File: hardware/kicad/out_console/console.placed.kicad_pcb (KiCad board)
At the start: 2 copper layers, 99.5 x 99.5 mm, 62 parts, among them J1 RaspberryPi_Pico_SMD_HandSold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, J10 JST_XH_B2B-XH-A_1x02_P2.50mm_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, J11 JST_XH_B2B-XH-A_1x02_P2.50mm_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, J12 JST_XH_B2B-XH-A_1x02_P2.50mm_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, J13 JST_XH_B2B-XH-A_1x02_P2.50mm_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, J14 JST_XH_B2B-XH-A_1x02_P2.50mm_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, J15 JST_XH_B2B-XH-A_1x02_P2.50mm_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, J16 JST_XH_B2B-XH-A_1x02_P2.50mm_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, J17 JST_XH_B2B-XH-A_1x02_P2.50mm_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, J18 JST_XH_B2B-XH-A_1x02_P2.50mm_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, J19 JST_XH_B2B-XH-A_1x02_P2.50mm_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, J2 IDC-Header_2x20_P2.54mm_Verti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, J20 JST_XH_B3B-XH-A_1x03_P2.50mm_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, J21 JST_XH_B3B-XH-A_1x03_P2.50mm_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, J22 PinHeader_2x04_P2.54mm_Vertic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, J3 JST_XH_B4B-XH-A_1x04_P2.50mm_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, J4 JST_XH_B3B-XH-A_1x03_P2.50mm_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, J5 JST_XH_B2B-XH-A_1x02_P2.50mm_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, J6 JST_XH_B4B-XH-A_1x04_P2.50mm_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, J7 JST_XH_B3B-XH-A_1x03_P2.50mm_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, J8 JST_XH_B2B-XH-A_1x02_P2.50mm_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, J9 JST_XH_B2B-XH-A_1x02_P2.50mm_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, U1 DIP-14_W7.62mm, U2 DIP-6_W7.62mm

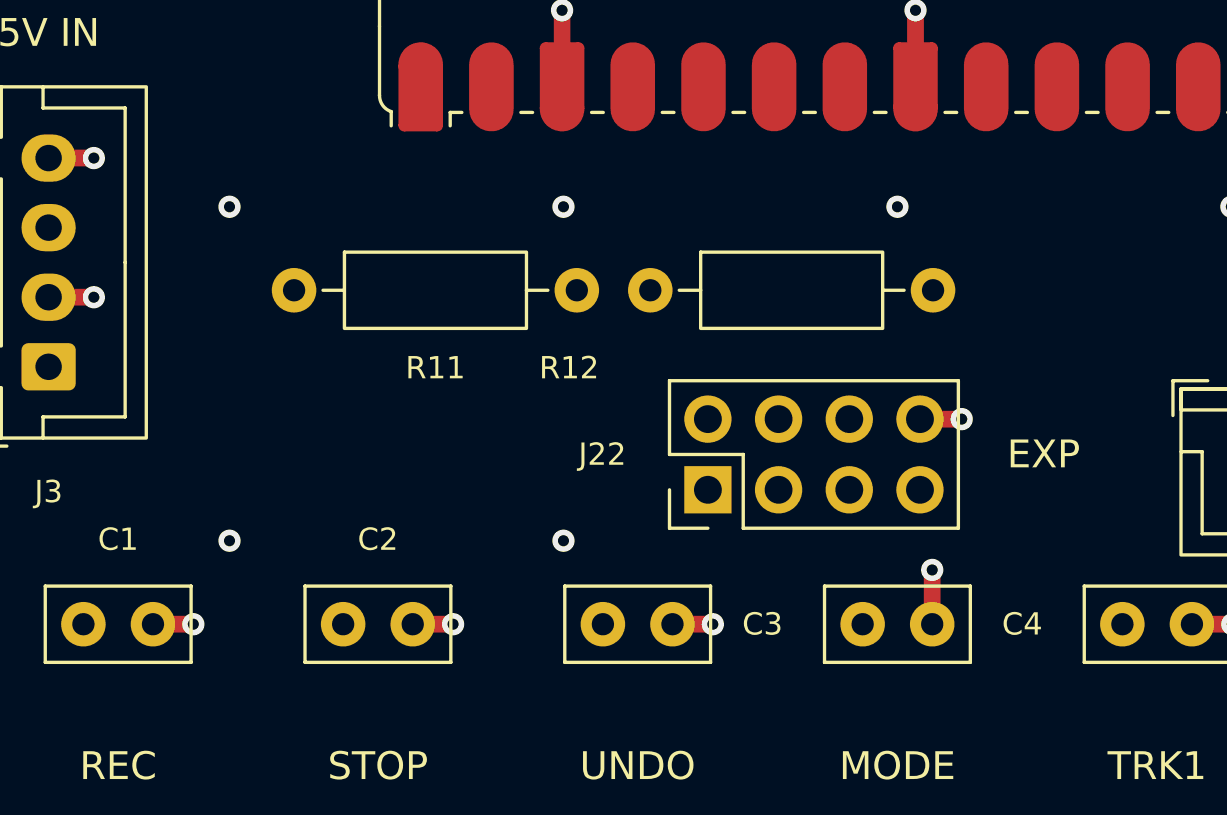
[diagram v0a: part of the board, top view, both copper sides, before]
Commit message: feat(hardware): console board v3 — read the PD trigger's contract over I2C
The console cannot tell whether the STUSB4500 negotiated 20 V / 5 A or a
65 W brick's 20 V / 3.25 A: both boot, and the second browns out only when
the LEDs go white under two lit screens. The chip is I2C-readable (RDO at
0x91-0x94 with capaMismatch, voltage at 0x21), so v3 gives it a header.

J23 PD: JST-XH 3-way — GND, SDA, SCL on GP0/GP1 (I2C0, the pins v2 left
spare), under the module's left end beside 5V IN; R11/R12 rise 3 mm to make
the row. Three wires on purpose: the breakout's VDD and pull-ups come off
VBUS on its own board, and this board's 3V3 is downstream of the contract
being measured. A gate now asserts the pair is one I2C instance's SDA/SCL,
and no GPIO on the module is spare any more (the UART self-test that leaned
on GP1 being free swaps pins instead).

Routed clean: 0 DRC violations, 0 unconnected, ratsnest 1725 mm of 1770.
Silk keep-outs and back art regenerated for the new pad set.

Firmware for the read and its pedal-link report is not written yet; the
wiring doc, the soldering guide's v3 table and the firmware README say so.
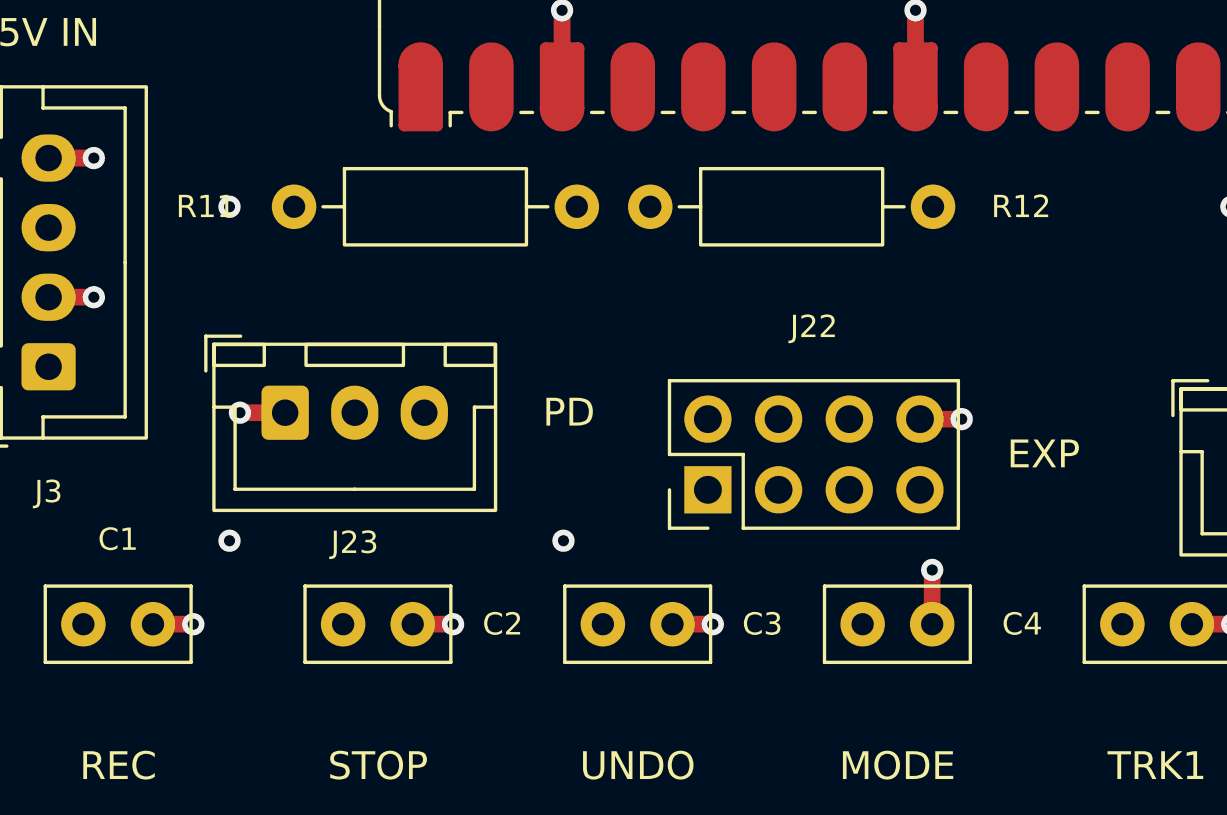
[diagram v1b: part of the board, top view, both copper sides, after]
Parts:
- added J23: JST_XH_B3B-XH-A_1x03_P2.50mm_Vertical, JST_XH_B3B-XH-A_1x03_P2.50mm_Vertical, F.Cu at (114.0, 127.4)
- moved R11 3.00 mm to (114.3, 120.0)
- moved R12 3.00 mm to (127.1, 120.0)
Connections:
- J1 pad 1: (no net) -> PD_SDA
- J1 pad 2: (no net) -> PD_SCL
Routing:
- net GND: track 117.8 -> 119.4 mm, vias 75 -> 74
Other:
- board text added: "PD"

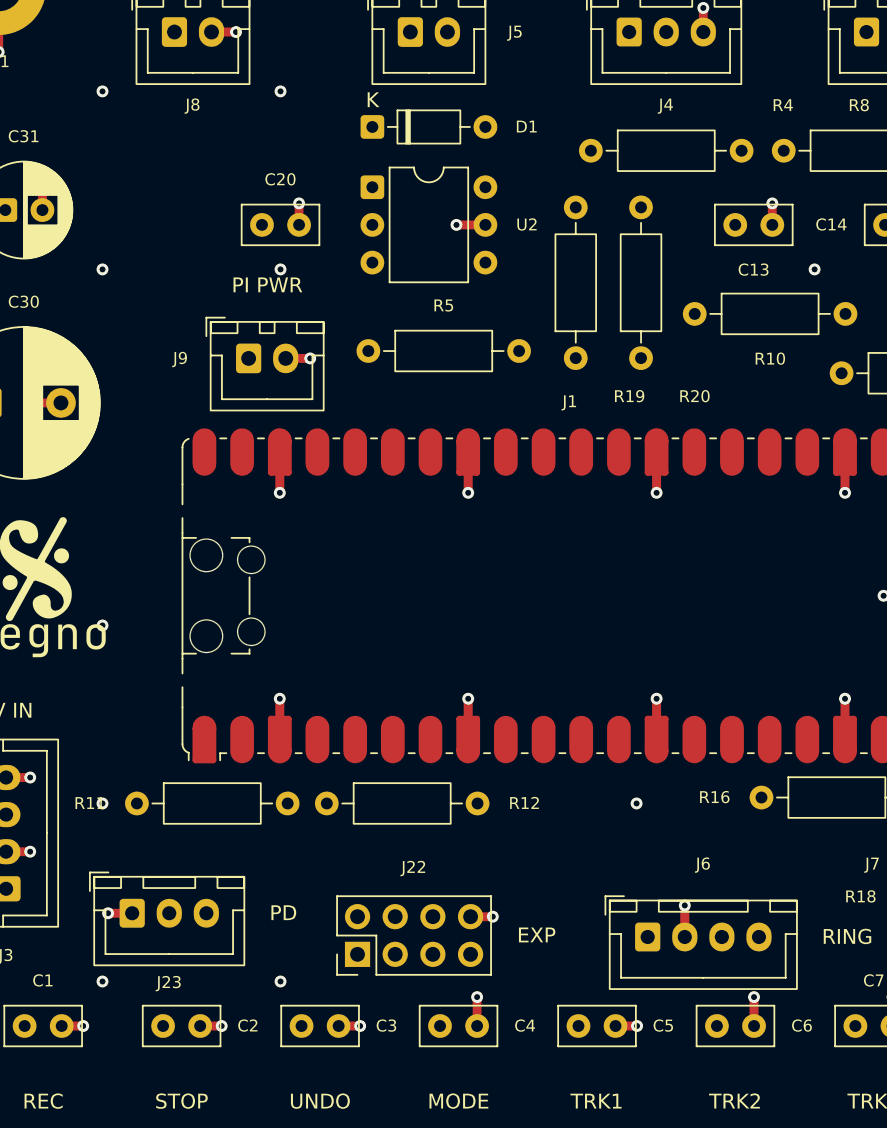
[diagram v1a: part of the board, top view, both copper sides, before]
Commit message: fix(hardware): v3 — EXP back where v2 had it, PD in the RING row
Bench feedback on the v3 layout: the expansion header was liked where v2 put
it, and the PD header sat 1.6 mm above the row it belongs to.

J22 returns to the column beside U2. R19/R20, which had taken that column
to stay under the jacks, move to the row R13 and R15 left empty under the
module; their nets are DC sense lines through 4.7 k, so the 50-60 mm run
does not matter, and the hop gate exempts them by name with that reason
(SLOW_SENSE_NETS). J23 drops onto the RING/LEDS row.

The silk keep-out list now covers every pad that opens the back mask, not
only plated ones: the Pico's three NPTH anchors were missed and the big
segno landed on them (silk_over_copper). Routed clean: 0 violations,
0 unconnected, ratsnest 1707 mm of 1770. Gerbers regenerated.
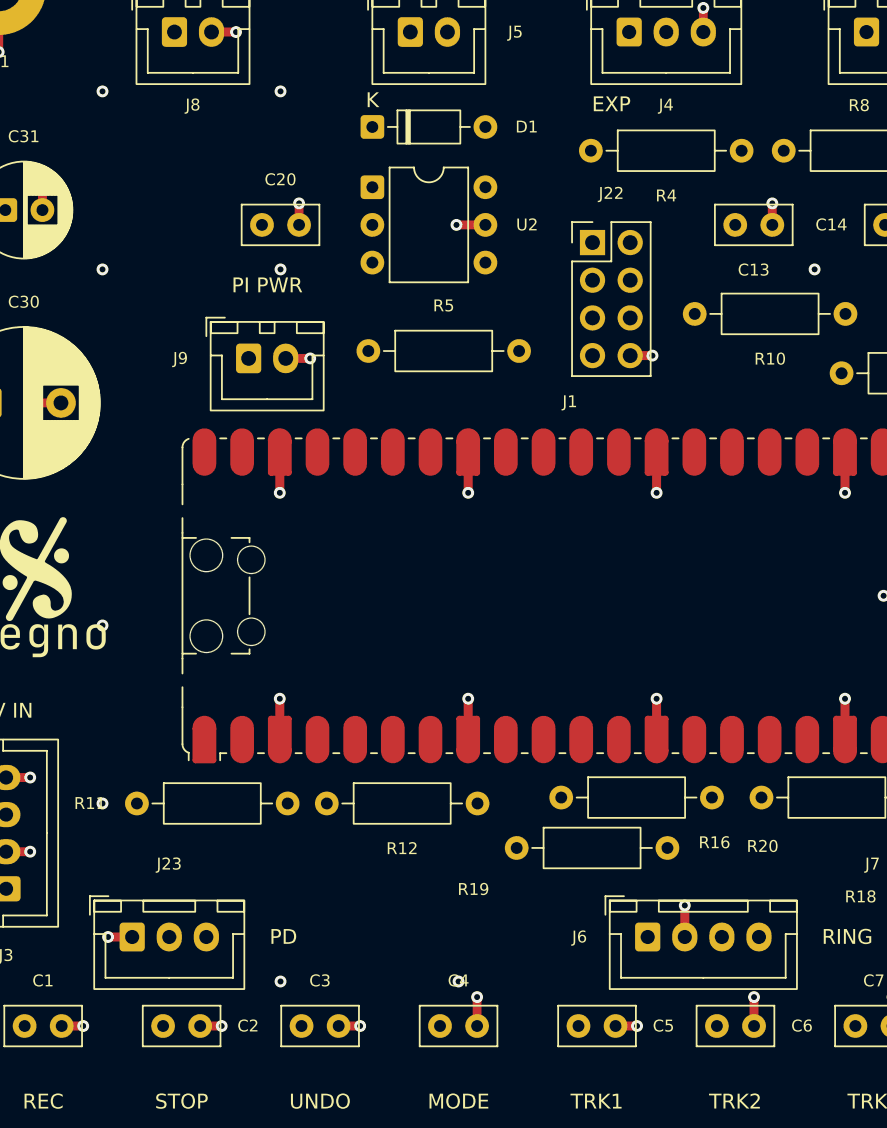
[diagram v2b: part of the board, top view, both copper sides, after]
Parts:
- moved J22 50.5 mm to (145.0, 82.2), turned to 0 degrees
- moved R19 33.3 mm to (139.9, 123.0), turned to 0 degrees
- moved R20 30.1 mm to (142.9, 119.6), turned to 0 degrees
- moved J23 1.60 mm to (114.0, 129.0)
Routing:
- net GND: vias 74 -> 73

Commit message: feat(hardware): console board v3 — switched CTRL jacks report presence
The CTRL jacks become Neutrik NJ6FD-V: D-series like the jack they
replace, same Ø24 punch and M3 pair, with switching contacts. Each jack's
tip-normal contact goes to the board as a fourth lead (J20/J21 are 4-way
now) and through 4.7 k (R21/R22) to GP19/GP22. The contact ties to the
tip — 3V3 through 10 k — while the jack is empty and opens once a plug is
in, so with the RP2350's pull-down the pin is high only for an empty jack.
Presence becomes a wire: an empty jack no longer reads as a pedal at full
toe, and a plug on its way in is ignored until it is seated. Firmware 1.2
reads it; on a v2 board the same pins float on J22's pads and read
"plugged", so one firmware serves both.

GP19/GP22 leave J22, which is 2x3 (GP12, GP15, GP28). The CTRL headers
slide 2.6 mm left to keep their clearances at 4-way width; R11/R12 join
R16/R20 on the band under the module so the row below is R21/R22's.

Ratsnest 1915 mm: the four sense nets run 50-60 mm to parts under the
module by decision (DC through 4.7 k, exempt from the hop gate), so the
budget follows the measurement to 2050 with that reason next to it. Routed
clean: 0 violations, 0 unconnected. Gerbers, BOM and art regenerated.

Docs: shopping list (NJ6FD-V x2, four leads), soldering guide's v3 table,
wiring, firmware README pin table.
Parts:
- added R21: R_Axial_DIN0207_L6.3mm_D2.5mm_P10.16mm_Horizontal, R_Axial_DIN0207_L6.3mm_D2.5mm_P10.16mm_Horizontal, F.Cu at (111.9, 123.0)
- added R22: R_Axial_DIN0207_L6.3mm_D2.5mm_P10.16mm_Horizontal, R_Axial_DIN0207_L6.3mm_D2.5mm_P10.16mm_Horizontal, F.Cu at (124.9, 123.0)
- J20, J21: value JST_XH_B3B-XH-A_1x03_P2.50mm_Vertical -> JST_XH_B4B-XH-A_1x04_P2.50mm_Vertical; footprint JST_XH_B3B-XH-A_1x03_P2.50mm_Vertical -> JST_XH_B4B-XH-A_1x04_P2.50mm_Vertical
- J22: value PinHeader_2x04_P2.54mm_Vertical -> PinHeader_2x03_P2.54mm_Vertical; footprint PinHeader_2x04_P2.54mm_Vertical -> PinHeader_2x03_P2.54mm_Vertical
- moved J20 3.85 mm to (159.7, 68.0)
- moved J21 1.55 mm to (173.9, 68.0)
- moved J22 1.27 mm to (145.0, 83.5)
- moved R11 0.40 mm to (114.3, 119.6)
- moved R12 0.40 mm to (127.1, 119.6)
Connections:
- J1 pad 25: EXP_GP19 -> CTRL1_PRESENT
- J1 pad 29: EXP_GP22 -> CTRL2_PRESENT
- J22 pad 5: EXP_GP19 -> EXP_GP28
- J22 pad 6: EXP_GP22 -> GND

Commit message: refactor(hardware): the issue numbers come off the console silkscreen
The bottom strip printed "SEGNO CONSOLE v3  #747 #987". Issue numbers are
provenance for whoever edits the generator, not for whoever solders the
board: a tracker is not something you can look up with a board in your
hand, and the numbers age worse than the board does. The title is now just
"SEGNO CONSOLE v3". They stay in the file's docstring and in
console_board_mount.json, which is where that context is useful.

_silk() takes the text CENTRE, so dropping the numbers only shortens the
title inward and its clearance to H4's pad can only improve; the SILK gates
re-measure it as rendered either way and pass.

Re-placed and re-routed to regenerate it: clean on the second attempt, 0
violations and 0 unconnected, fab checks PASS, all 96 vias 0.8/0.4. The
back-silk wordmark ("segno console board v3") never carried numbers, and
the ring board's silk is just "SEGNO RING", so neither needed touching.
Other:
- board text added: "SEGNO CONSOLE v3"
- board text removed: "SEGNO CONSOLE v3 #747 #987"

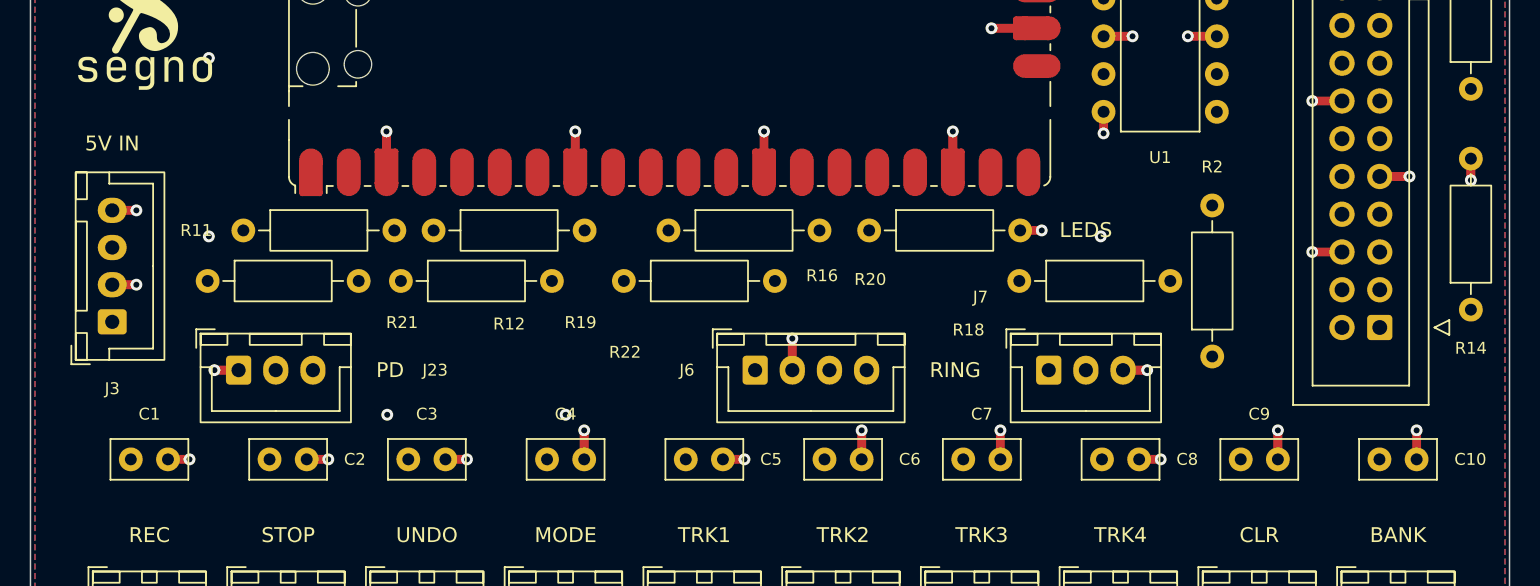
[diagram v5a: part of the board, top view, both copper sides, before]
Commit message: feat(hardware): console board 5 V path for full-white LEDs, and pre-order review fixes (#1062)
Console board v3:
- J3 (5 V in) becomes a 2-pin JST VH; the pills move to one 3-pin JST VH J24
  (GND, DATA, +5V) whose +5V pad is bridged to J3's by a poured bar on both
  layers; J7 is retired. PILL_POWER gates the topology.
- VH 3D models generated by vh_models.py.
- Per-pin legends on the back silkscreen for J3 and J24, which read in
  opposite orders; PIN_LEGEND gates them.
- Committed gerbers and STEP brought up to date with the routed board.

Ring board:
- R5 100k holds the AHCT125 input low while the XIAO is not driving it, so
  the ring cannot latch random colours at power-up; RING_DATA_IDLE gates it.
- Rerouted, DRC clean, gerbers and STEP regenerated.
- The combined LCSC BOM describes the XIAO ring board instead of the old one.
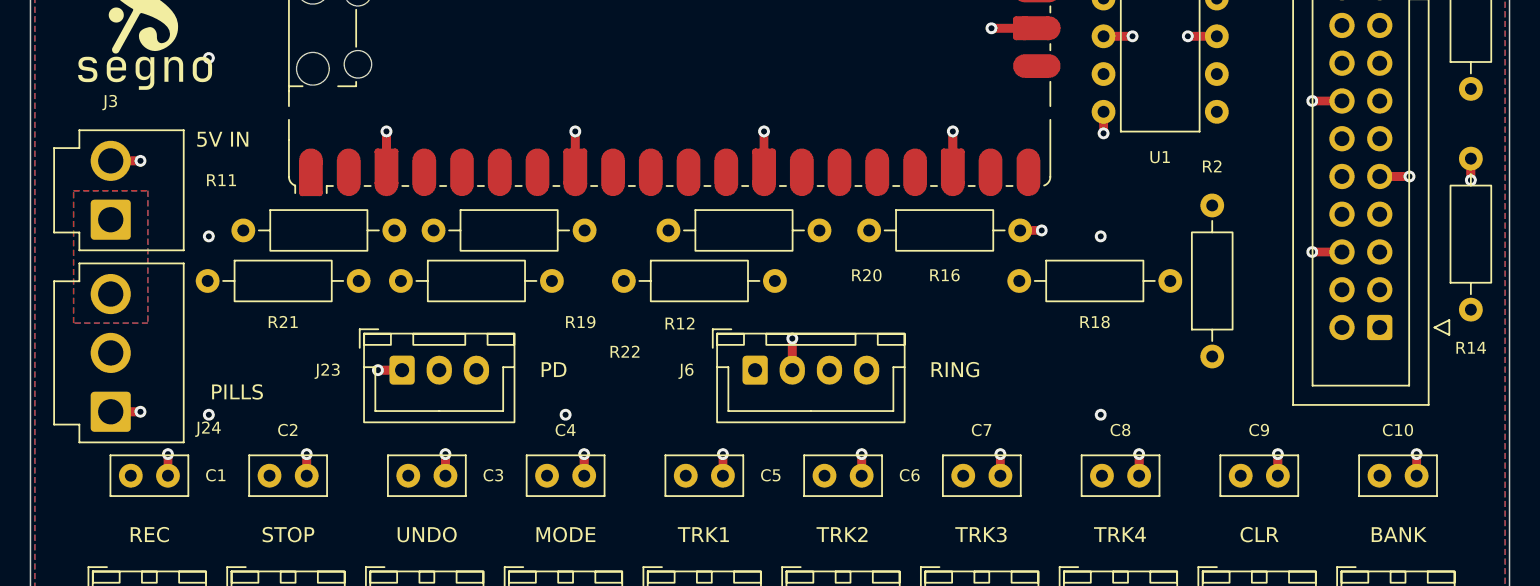
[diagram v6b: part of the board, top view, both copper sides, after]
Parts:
- removed J7: JST_XH_B3B-XH-A_1x03_P2.50mm_Vertical, JST_XH_B3B-XH-A_1x03_P2.50mm_Vertical
- added J24: JST_VH_B3P-VH_1x03_P3.96mm_Vertical, JST_VH_B3P-VH_1x03_P3.96mm_Vertical, F.Cu at (105.4, 131.8)
- J3: value JST_XH_B4B-XH-A_1x04_P2.50mm_Vertical -> JST_VH_B2P-VH_1x02_P3.96mm_Vertical; footprint JST_XH_B4B-XH-A_1x04_P2.50mm_Vertical -> JST_VH_B2P-VH_1x02_P3.96mm_Vertical
- moved J23 11.0 mm to (125.0, 129.0)
- moved J3 6.87 mm to (105.4, 118.9)
- moved C1 1.10 mm to (106.8, 136.1)
- moved C10 1.10 mm to (190.8, 136.1)
- moved C2 1.10 mm to (116.1, 136.1)
- moved C3 1.10 mm to (125.4, 136.1)
- moved C4 1.10 mm to (134.8, 136.1)
- moved C5 1.10 mm to (144.1, 136.1)
- moved C6 1.10 mm to (153.4, 136.1)
- moved C7 1.10 mm to (162.8, 136.1)
- moved C8 1.10 mm to (172.1, 136.1)
- moved C9 1.10 mm to (181.4, 136.1)
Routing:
- net GND: track 119.4 -> 116.0 mm
- added copper zone on B.Cu, net +5V
- added copper zone on F.Cu, net +5V
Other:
- board text added: "+5V"
- board text added: "DATA"
- board text added: "GND"
- board text added: "PILLS"
- board text removed: "LEDS"
